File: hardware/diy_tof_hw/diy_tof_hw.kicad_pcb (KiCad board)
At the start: 2 copper layers, 100 x 100 mm, 50 parts, among them IC1 TDC7200PWR, IC2 TDC7200PWR, IC21 74LVC1G08QW5-7, IC22 LMG1025QDEETQ1, J1 Conn_01x02_Pin, J2 Conn_01x03_Pin, J3 Conn_01x02_Pin, SW1 SW_Nidec_CAS-120A1, SW2 SW_Nidec_CAS-120A1, U1 NUCLEO-F042K6, U2 OPA858xDSG, U3 TLV3501AIDBV, X1 SG-5032CAN

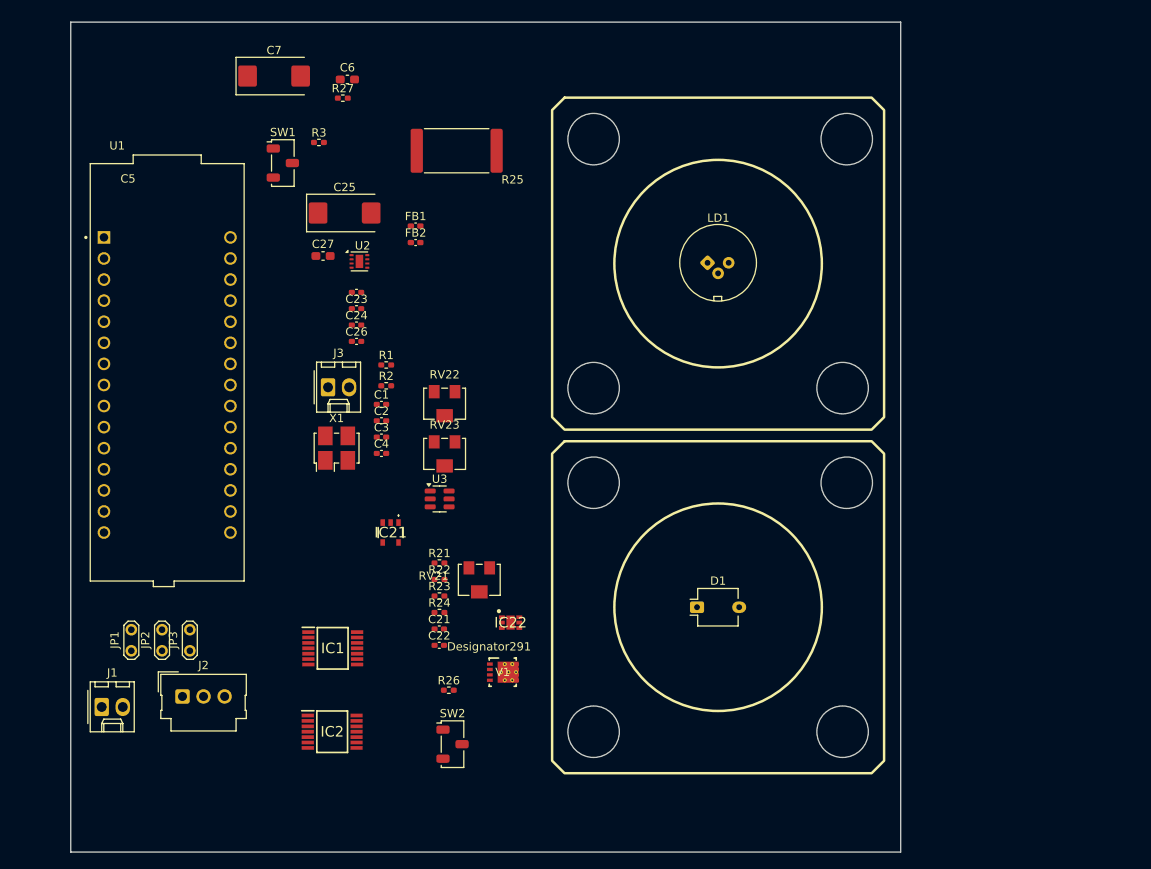
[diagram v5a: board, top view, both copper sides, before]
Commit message: [hardware] added various testpoints, some minor other fixes on the layout (designators)
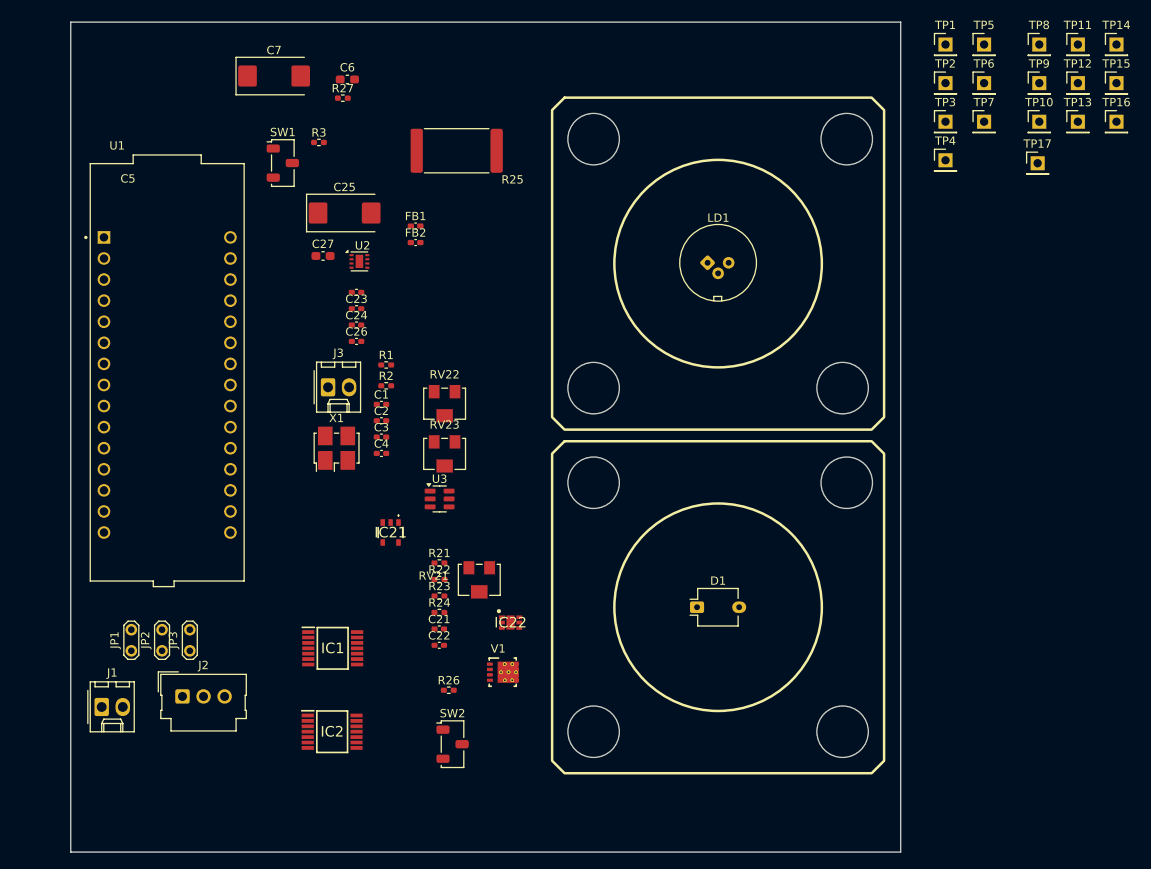
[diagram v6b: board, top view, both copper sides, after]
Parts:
- added TP1: Conn_01x01_Pin, Connector_PinHeader_2.54mm:PinHeader_1x01_P2.54mm_Vertical, F.Cu at (151.4, 32.7)
- added TP10: Conn_01x01_Pin, Connector_PinHeader_2.54mm:PinHeader_1x01_P2.54mm_Vertical, F.Cu at (162.7, 42.0)
- added TP11: Conn_01x01_Pin, Connector_PinHeader_2.54mm:PinHeader_1x01_P2.54mm_Vertical, F.Cu at (167.3, 32.7)
- added TP12: Conn_01x01_Pin, Connector_PinHeader_2.54mm:PinHeader_1x01_P2.54mm_Vertical, F.Cu at (167.3, 37.4)
- added TP13: Conn_01x01_Pin, Connector_PinHeader_2.54mm:PinHeader_1x01_P2.54mm_Vertical, F.Cu at (167.3, 42.0)
- added TP14: Conn_01x01_Pin, Connector_PinHeader_2.54mm:PinHeader_1x01_P2.54mm_Vertical, F.Cu at (172.0, 32.7)
- added TP15: Conn_01x01_Pin, Connector_PinHeader_2.54mm:PinHeader_1x01_P2.54mm_Vertical, F.Cu at (172.0, 37.4)
- added TP16: Conn_01x01_Pin, Connector_PinHeader_2.54mm:PinHeader_1x01_P2.54mm_Vertical, F.Cu at (172.0, 42.0)
- added TP17: Conn_01x01_Pin, Connector_PinHeader_2.54mm:PinHeader_1x01_P2.54mm_Vertical, F.Cu at (162.5, 47.0)
- added TP2: Conn_01x01_Pin, Connector_PinHeader_2.54mm:PinHeader_1x01_P2.54mm_Vertical, F.Cu at (151.4, 37.4)
- added TP3: Conn_01x01_Pin, Connector_PinHeader_2.54mm:PinHeader_1x01_P2.54mm_Vertical, F.Cu at (151.4, 42.0)
- added TP4: Conn_01x01_Pin, Connector_PinHeader_2.54mm:PinHeader_1x01_P2.54mm_Vertical, F.Cu at (151.4, 46.6)
- added TP5: Conn_01x01_Pin, Connector_PinHeader_2.54mm:PinHeader_1x01_P2.54mm_Vertical, F.Cu at (156.1, 32.7)
- added TP6: Conn_01x01_Pin, Connector_PinHeader_2.54mm:PinHeader_1x01_P2.54mm_Vertical, F.Cu at (156.1, 37.4)
- added TP7: Conn_01x01_Pin, Connector_PinHeader_2.54mm:PinHeader_1x01_P2.54mm_Vertical, F.Cu at (156.1, 42.0)
- added TP8: Conn_01x01_Pin, Connector_PinHeader_2.54mm:PinHeader_1x01_P2.54mm_Vertical, F.Cu at (162.7, 32.7)
- added TP9: Conn_01x01_Pin, Connector_PinHeader_2.54mm:PinHeader_1x01_P2.54mm_Vertical, F.Cu at (162.7, 37.4)
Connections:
- net /Power_Nucleo/12_nuc renamed /Power_Nucleo_TDC/12_nuc
- net /Power_Nucleo/TDC_ele_enable renamed /Power_Nucleo_TDC/TDC_ele_enable
- net /Power_Nucleo/TDC_opt_enable renamed /Power_Nucleo_TDC/TDC_opt_enable
- net /Power_Nucleo/clk_tdc renamed /Power_Nucleo_TDC/clk_tdc
- net /Power_Nucleo/int_ele renamed /Power_Nucleo_TDC/int_ele
- net /Power_Nucleo/int_opt renamed /Power_Nucleo_TDC/int_opt
- net /Power_Nucleo/spi_clk renamed /Power_Nucleo_TDC/spi_clk
- net /Power_Nucleo/spi_cs_ele renamed /Power_Nucleo_TDC/spi_cs_ele
- net /Power_Nucleo/spi_cs_opt renamed /Power_Nucleo_TDC/spi_cs_opt
- net /Power_Nucleo/spi_miso renamed /Power_Nucleo_TDC/spi_miso
- net /Power_Nucleo/spi_mosi renamed /Power_Nucleo_TDC/spi_mosi
- net /Power_Nucleo/start_ele renamed /Power_Nucleo_TDC/start_ele
- net /Power_Nucleo/start_opt renamed /Power_Nucleo_TDC/start_opt
- net /Power_Nucleo/stop_ele renamed /Power_Nucleo_TDC/stop_ele
- IC1 pad 2: unconnected-(IC1-TRIGG-Pad2) -> Net-(IC1-TRIGG)
- IC2 pad 2: unconnected-(IC2-TRIGG-Pad2) -> Net-(IC2-TRIGG)

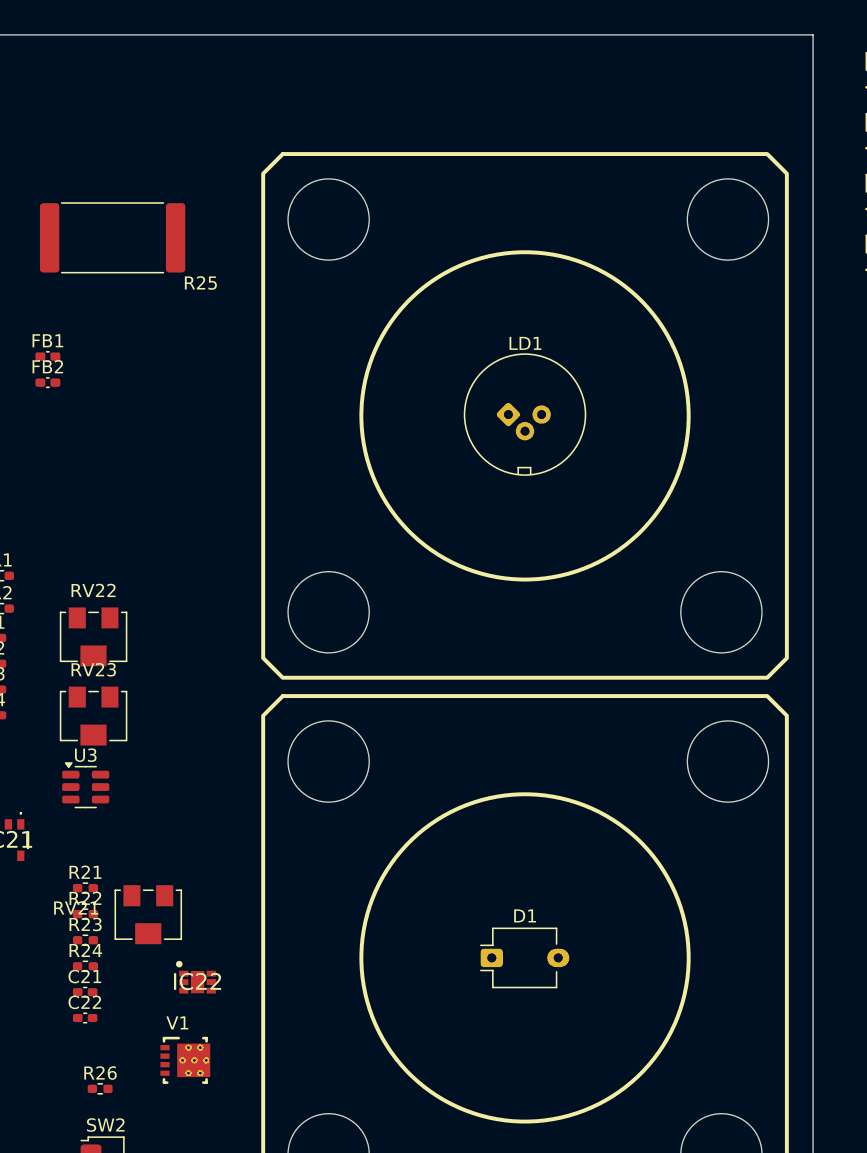
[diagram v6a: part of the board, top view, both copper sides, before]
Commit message: [hardware] added VCSEL, photodiode and some pcb graphics to the project
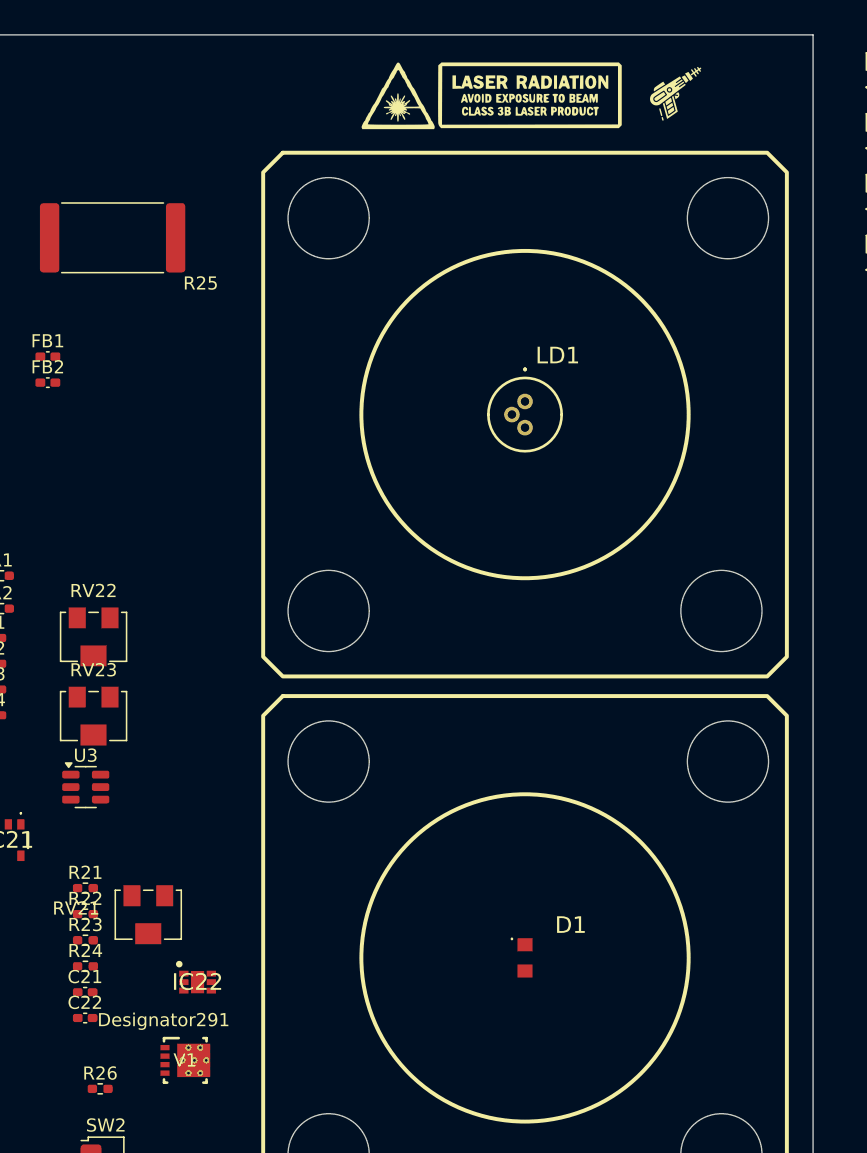
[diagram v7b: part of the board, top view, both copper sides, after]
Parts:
- added G***: LOGO, LOGO, F.Cu at (135.5, 34.5)
- added G***: LOGO, graphics:laser_hazard, F.Cu at (121.5, 34.5)
- D1: value BPW34 -> NJL6401R-3-TE1; footprint OptoDevice:Osram_DIL2_4.3x4.65mm_P5.08mm -> NJL6401R-3-TE1:NJL6401R3TE1
- LD1: value D_Laser_Photo_MType -> ~; footprint OptoDevice:LaserDiode_TO5-D9-3 -> RLD65NZX1-00A:RLD85PZJ400A
- moved D1 2.54 mm to (124.0, 100.5)
- moved LD1 1.62 mm to (124.0, 58.0)
- moved X2 0.10 mm to (124.0, 59.0)
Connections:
- D1 pad 1: Net-(D1-K) -> Net-(D1-A)
- D1 pad 2: Net-(D1-A) -> Net-(D1-K)
- LD1 pad 1: Net-(TP9-Pin_1) -> Net-(LD1-Pad1)
- LD1 pad 2: Net-(LD1-Pad2) -> unconnected-(LD1-Pad2)
- LD1 pad 3: unconnected-(LD1-Pad3) -> Net-(TP9-Pin_1)
- V1 pad 5: Net-(LD1-Pad2) -> Net-(LD1-Pad1)
- V1 pad 6: Net-(LD1-Pad2) -> Net-(LD1-Pad1)
- V1 pad 7: Net-(LD1-Pad2) -> Net-(LD1-Pad1)
- V1 pad 8: Net-(LD1-Pad2) -> Net-(LD1-Pad1)
